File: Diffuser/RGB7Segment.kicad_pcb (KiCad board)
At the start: 2 copper layers, 15.2 x 14.9 mm, 2 parts, among them J1 Conn_01x02_Socket, J2 Conn_01x02_Socket

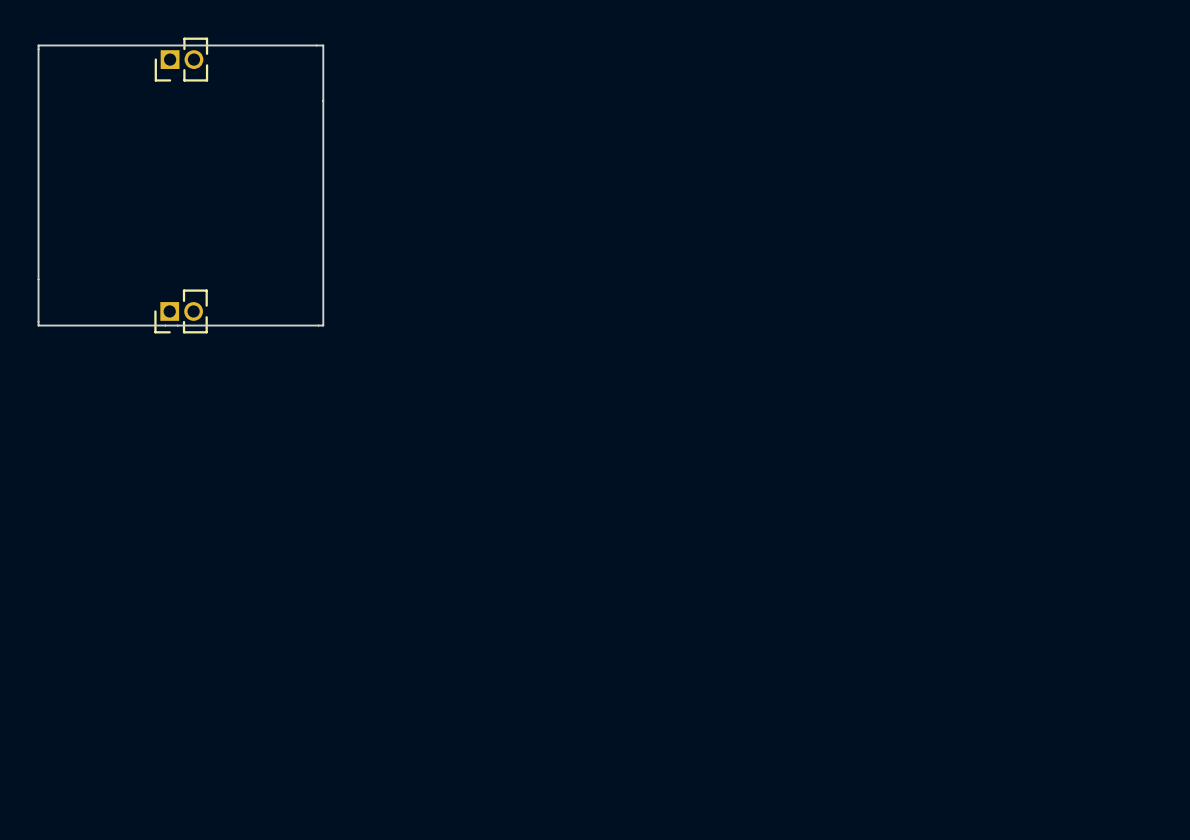
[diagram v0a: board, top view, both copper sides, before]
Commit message: Working 7 Segment Layout
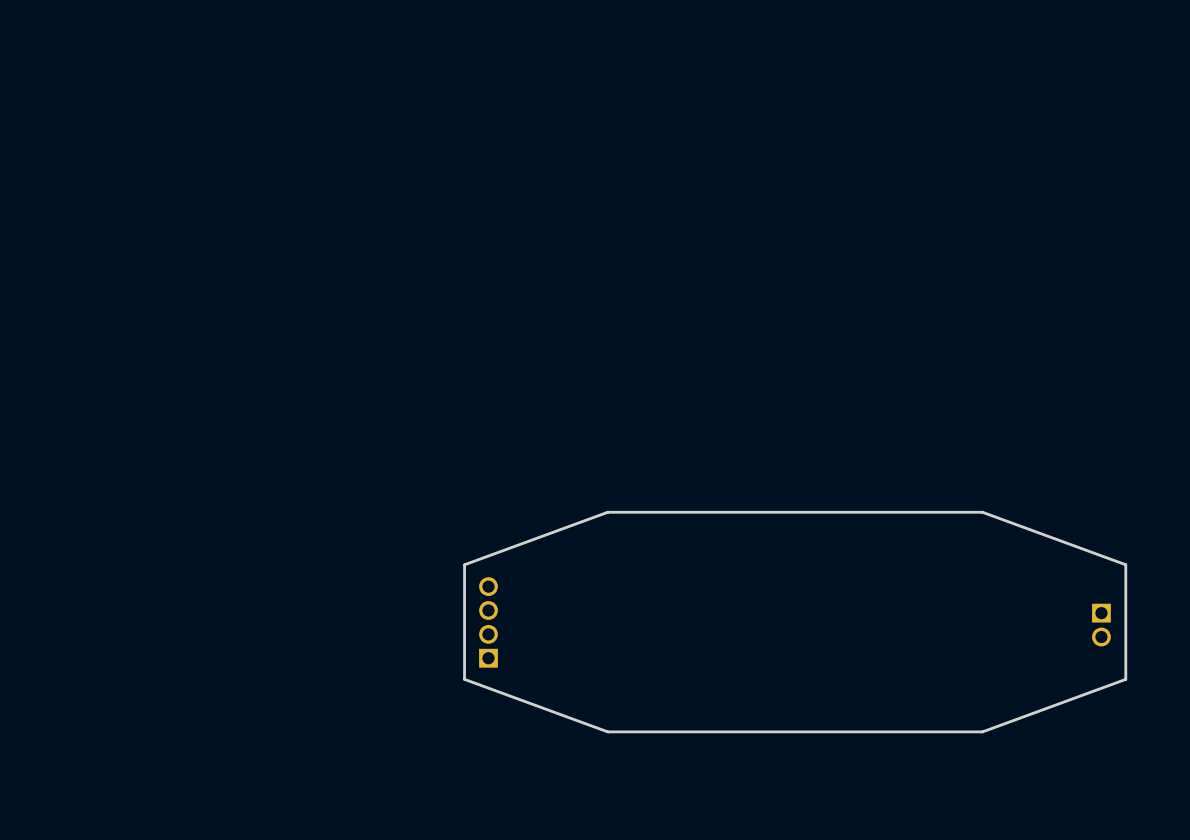
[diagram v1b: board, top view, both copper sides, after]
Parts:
- J1: moved to B.Cu
- J2: value Conn_01x02_Socket -> Conn_01x04_Pin; footprint Connector_PinHeader_1.27mm:PinHeader_1x02_P1.27mm_Vertical -> Connector_PinHeader_1.27mm:PinHeader_1x04_P1.27mm_Vertical; moved to B.Cu
- moved J1 57.6 mm to (250.8, 106.0), turned to 180 degrees
- moved J2 25.1 mm to (218.2, 108.4), turned to 0 degrees
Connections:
- J2 pad 1: /DIN -> /DOUT
- J2 pad 2: /DOUT -> /COUT
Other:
- board size 15.2 x 14.9 mm -> 35.2 x 11.7 mm

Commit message: New Layout for diffuser. Needs further direction.
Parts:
- moved J1 1.47 mm to (252.1, 105.3)
- moved J2 1.47 mm to (219.5, 107.7)
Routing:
- added copper zone on B.Cu, net GND
- added copper zone on F.Cu, net GND
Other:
- board size 35.2 x 11.7 mm -> 35.2 x 19.1 mm
- board text added: "GND"
- board text added: "VCC"

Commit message: New Minor Layout
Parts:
- added J2: Conn_01x04_Pin, Connector_PinHeader_1.27mm:PinHeader_1x04_P1.27mm_Vertical, B.Cu at (219.5, 107.7)
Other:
- board size 35.2 x 19.1 mm -> 35.2 x 21.4 mm
